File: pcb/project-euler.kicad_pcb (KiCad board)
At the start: 4 copper layers, 34 x 32.5 mm, 63 parts, among them J1 USB_C_Receptacle_USB2.0_16P, J2 JST_ZH, J3 Conn_01x06, U1 FT201XQ, U2 BQ25186, U3 TLV75533PDBV, U4 ESP32-C6-WROOM-1, U5 BNO08x

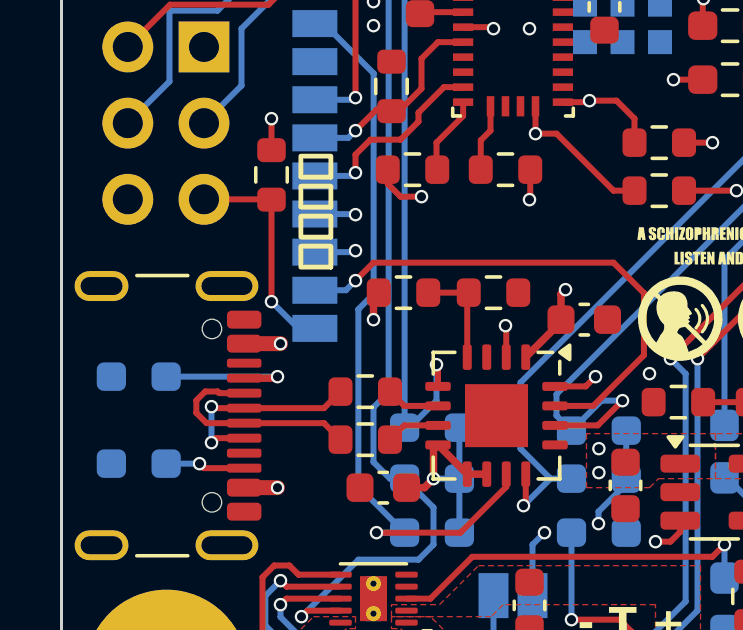
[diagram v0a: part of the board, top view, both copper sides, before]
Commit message: [firmware/pcb] Initial firmware upload + fixed mistake in PCB + added errata documentation
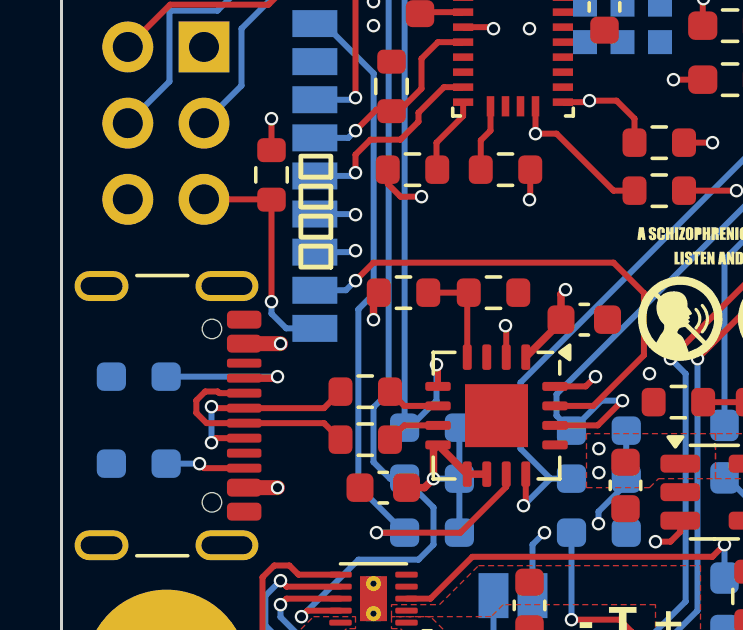
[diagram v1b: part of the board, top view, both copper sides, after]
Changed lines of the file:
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@@
 		(sheetname "/IMU/")
 		(sheetfile "imu.kicad_sch")
-		(attr smd)
+		(attr smd dnp)
 		(fp_line
 			(start -0.237258 -0.5225)
@@
 	)
 	(segment
+		(start 41.99 51.59)
+		(end 41.5 51.1)
+		(width 0.2)
+		(layer "B.Cu")
+		(net 16)
+	)
+	(segment
 		(start 42.945 51.59)
-		(end 42.39 51.59)
+		(end 41.99 51.59)
 		(width 0.2)
 		(layer "B.Cu")
@@
 	)
 	(segment
-		(start 42.39 51.59)
+		(start 41.5 51.1)
 		(end 41.5 50.7)
 		(width 0.2)
